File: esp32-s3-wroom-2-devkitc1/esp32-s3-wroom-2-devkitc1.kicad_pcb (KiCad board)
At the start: 2 copper layers, 68.6 x 61 mm, 2 parts

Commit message: gen gerbers
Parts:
- removed LORA: lora-adafruit, maciek-lib:lora-adafruit
- added REF**: MountingHole_2.2mm_M2_DIN965_Pad, MountingHole:MountingHole_2.2mm_M2_DIN965_Pad, F.Cu at (180.3, 114.3)
- added REF**: MountingHole_2.2mm_M2_DIN965_Pad, MountingHole:MountingHole_2.2mm_M2_DIN965_Pad, F.Cu at (180.3, 58.4)
- added REF**: MountingHole_2.2mm_M2_DIN965_Pad, MountingHole:MountingHole_2.2mm_M2_DIN965_Pad, F.Cu at (116.8, 58.4)
- added REF**: MountingHole_2.2mm_M2_DIN965_Pad, MountingHole:MountingHole_2.2mm_M2_DIN965_Pad, F.Cu at (116.8, 114.3)
- added RFM95W1: ~, maciek-lib:lora-adafruit, F.Cu at (149.9, 101.6)
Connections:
- REF** pad 1: (no net) -> GND
- REF** pad 21: (no net) -> GND
- REF** pad 22: (no net) -> GND
- REF** pad 23: (no net) -> +3.3V
- REF** pad 24: (no net) -> +3.3V
- REF** pad 44: (no net) -> GND
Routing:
- net (no net): track 320.0 -> 0.00 mm
- net unconnected-(RFM95W1-Pad6): track 0.00 -> 71.0 mm
- net unconnected-(RFM95W1-Pad14): track 0.00 -> 62.0 mm
- net +3.3V: track 0.00 -> 49.3 mm
- net unconnected-(RFM95W1-Pad4): track 0.00 -> 32.6 mm
- net unconnected-(RFM95W1-Pad5): track 0.00 -> 26.5 mm
- net unconnected-(RFM95W1-Pad2): track 0.00 -> 23.9 mm
- net unconnected-(RFM95W1-Pad3): track 0.00 -> 23.9 mm
- net unconnected-(RFM95W1-Pad1): track 0.00 -> 7.62 mm
- added copper zone on B.Cu, net GND

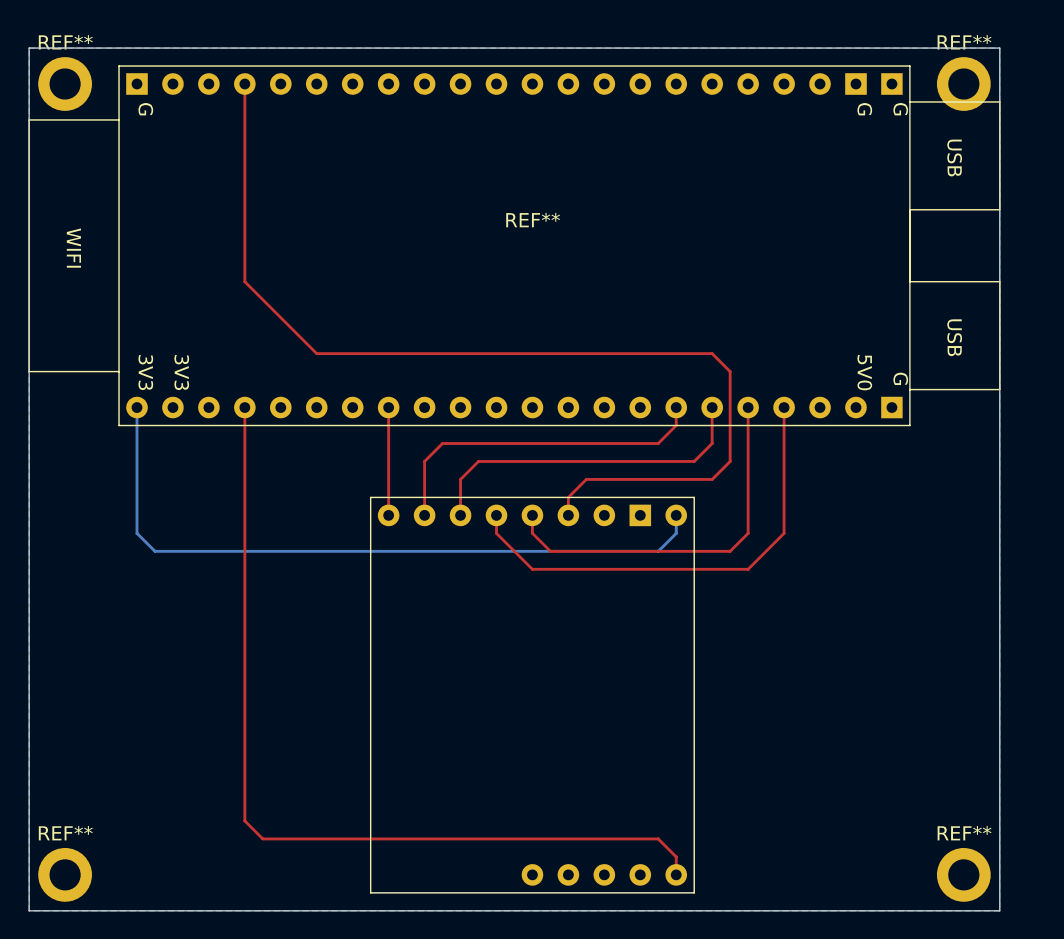
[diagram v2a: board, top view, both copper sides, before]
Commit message: add nests and 3v3 area
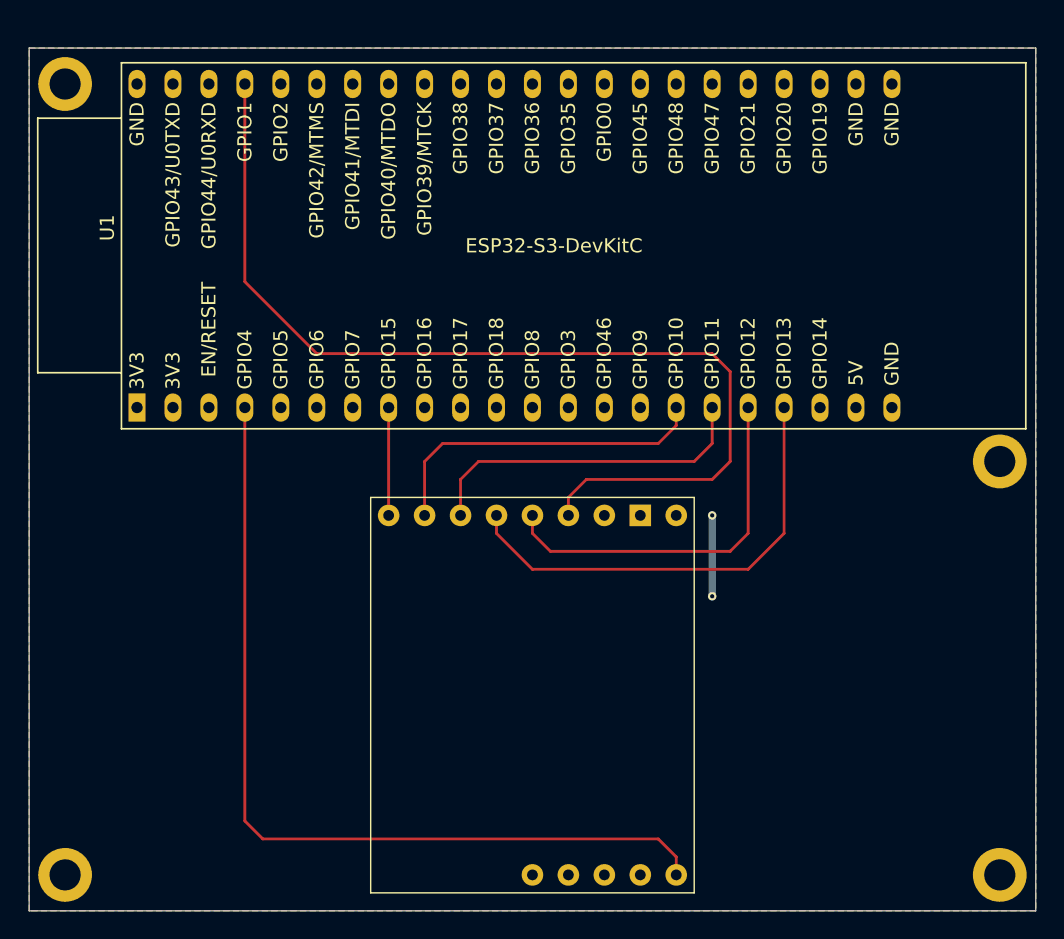
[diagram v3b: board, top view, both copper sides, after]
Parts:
- removed the REF** at (149.9, 68.6)
- added U1: ESP32-S3-DevKitC, PCM_Espressif:ESP32-S3-DevKitC, F.Cu at (121.9, 81.3)
- moved REF** 26.8 mm to (182.9, 85.1)
- moved REF** 2.54 mm to (182.9, 114.3)
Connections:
- RFM95W1 pad 1: unconnected-(RFM95W1-RST-Pad1) -> /RST
- RFM95W1 pad 14: unconnected-(RFM95W1-G1-Pad14) -> /G1
- RFM95W1 pad 2: unconnected-(RFM95W1-CS-Pad2) -> Net-(RFM95W1-CS)
- RFM95W1 pad 3: unconnected-(RFM95W1-MOSI-Pad3) -> Net-(RFM95W1-MOSI)
- RFM95W1 pad 4: unconnected-(RFM95W1-MISO-Pad4) -> Net-(RFM95W1-MISO)
- RFM95W1 pad 5: unconnected-(RFM95W1-SCK-Pad5) -> Net-(RFM95W1-SCK)
- RFM95W1 pad 6: unconnected-(RFM95W1-G0-Pad6) -> Net-(RFM95W1-G0)
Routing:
- net unconnected-(RFM95W1-G0-Pad6): track 71.0 -> 0.00 mm
- net Net-(RFM95W1-G0): track 0.00 -> 71.0 mm
- net unconnected-(RFM95W1-G1-Pad14): track 62.0 -> 0.00 mm
- net /G1: track 0.00 -> 62.0 mm
- net +3.3V: track 49.3 -> 5.71 mm, vias 0 -> 2
- net unconnected-(RFM95W1-MISO-Pad4): track 32.6 -> 0.00 mm
- net Net-(RFM95W1-MISO): track 0.00 -> 32.6 mm
- net unconnected-(RFM95W1-SCK-Pad5): track 26.5 -> 0.00 mm
- net Net-(RFM95W1-SCK): track 0.00 -> 26.5 mm
- net unconnected-(RFM95W1-CS-Pad2): track 23.9 -> 0.00 mm
- net Net-(RFM95W1-CS): track 0.00 -> 23.9 mm
- net unconnected-(RFM95W1-MOSI-Pad3): track 23.9 -> 0.00 mm
- net Net-(RFM95W1-MOSI): track 0.00 -> 23.9 mm
- net unconnected-(RFM95W1-RST-Pad1): track 7.62 -> 0.00 mm
- net /RST: track 0.00 -> 7.62 mm
- added copper zone on F.Cu, net +3.3V
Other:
- board size 68.6 x 61 mm -> 71.1 x 61 mm

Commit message: need bigger holes
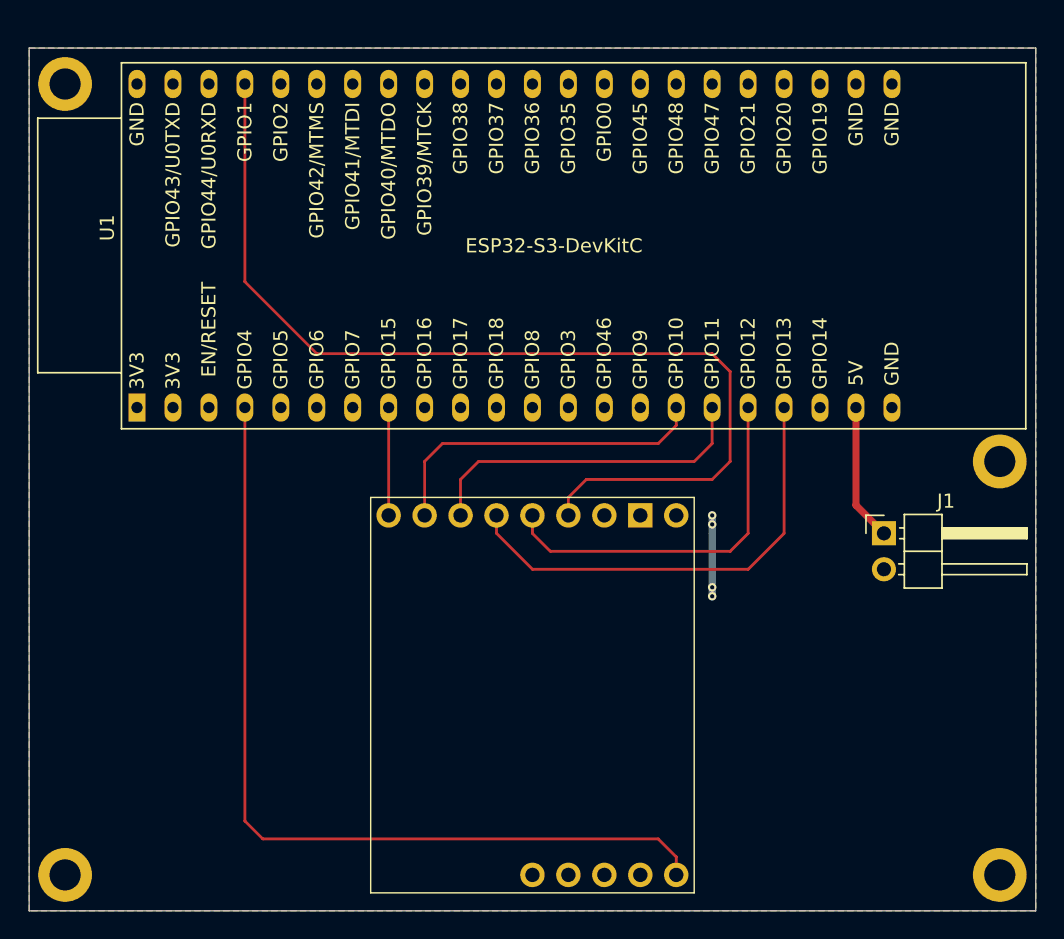
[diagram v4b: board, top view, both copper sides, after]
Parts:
- added J1: Conn_01x02_Pin, Connector_PinHeader_2.54mm:PinHeader_1x02_P2.54mm_Horizontal, F.Cu at (174.7, 90.2)
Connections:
- U1 pad 21: unconnected-(U1-5V-Pad21) -> +5V
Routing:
- net +5V: track 0.00 -> 9.70 mm
- net +3.3V: vias 2 -> 4
